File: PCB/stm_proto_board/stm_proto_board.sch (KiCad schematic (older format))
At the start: 35 parts, among them J1 Conn_01x08_Female, J2 Conn_01x04, J3 DB9_Female, J4 Conn_01x02, J5 Conn_01x04, SW1 SW_Push, SW2 SW_Push, SW3 SW_Push, SW4 SW_Push, U1 STM32F103C8T6_shield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

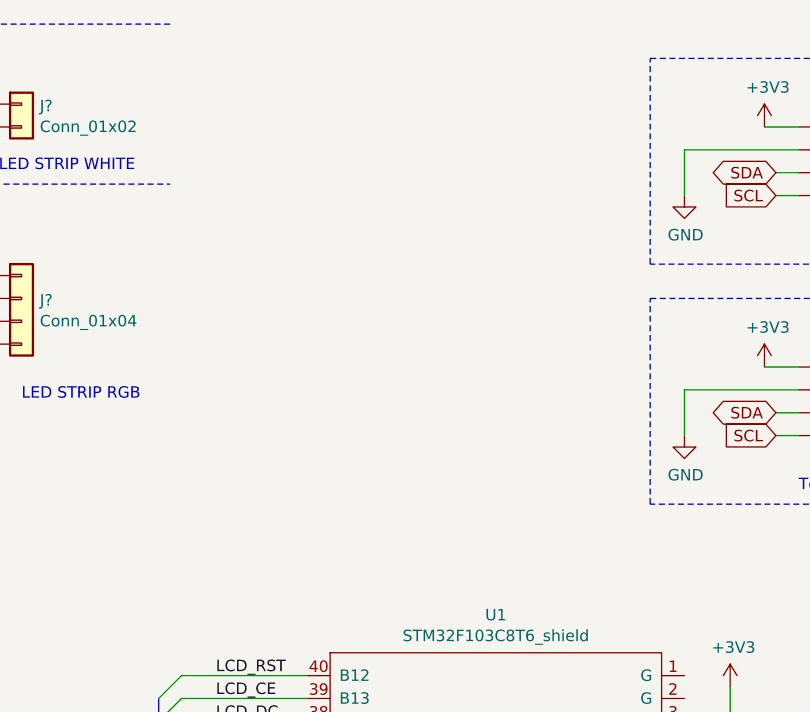
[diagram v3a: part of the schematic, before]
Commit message: Add enc28j60 on schematic + convert pinout in md format
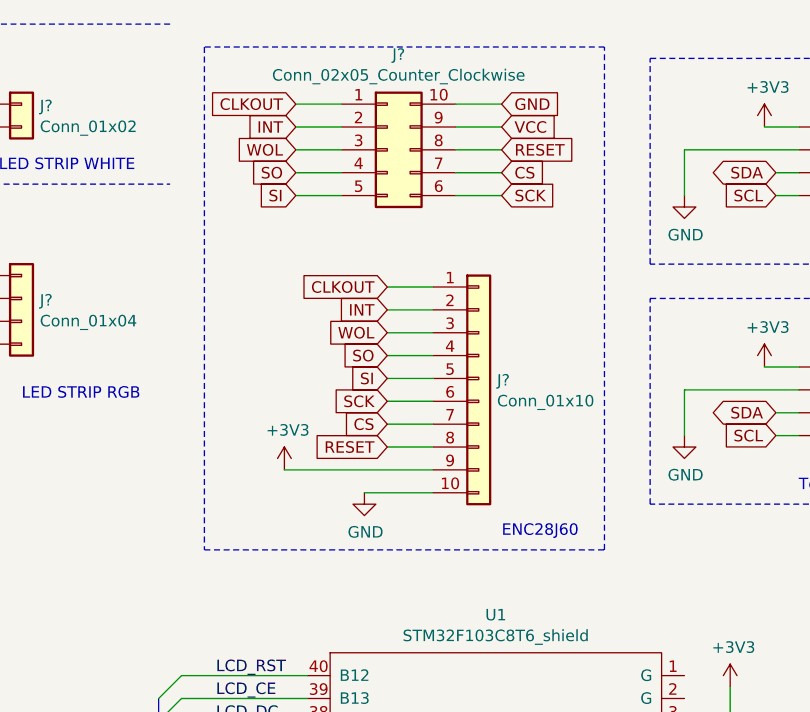
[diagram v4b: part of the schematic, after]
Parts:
- added J?: Conn_02x05_Counter_Clockwise, symbol Connector_Generic:Conn_02x05_Counter_Clockwise
- added J?: Conn_01x10, symbol Connector_Generic:Conn_01x10
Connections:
- net +3V3: now also J?.9 (Pin_9), J?.9 (Pin_9)
- net GND: now also J?.10 (Pin_10), J?.10 (Pin_10)
- new net CLKOUT: J?.1 (Pin_1), J?.1 (Pin_1)
- new net CS: J?.7 (Pin_7), J?.7 (Pin_7)
- new net INT: J?.2 (Pin_2), J?.2 (Pin_2)
- new net RESET: J?.8 (Pin_8), J?.8 (Pin_8)
- new net SCK: J?.6 (Pin_6), J?.6 (Pin_6)
- new net SI: J?.5 (Pin_5), J?.5 (Pin_5)
- new net SO: J?.4 (Pin_4), J?.4 (Pin_4)
- new net WOL: J?.3 (Pin_3), J?.3 (Pin_3)
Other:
- note added: "ENC28J60"
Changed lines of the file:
@@
 Wire Wire Line
 	1300 3050 1450 3050
-$Comp
-L power:GND #PWR0129
-U 1 1 5BB06CFC
-P 3200 2000
-F 0 "#PWR0129" H 3200 1750 50  0001 C CNN
-F 1 "GND" H 3205 1827 50  0000 C CNN
-F 2 "" H 3200 2000 50  0001 C CNN
-F 3 "" H 3200 2000 50  0001 C CNN
-	1    3200 2000
-	1    0    0    -1
-$EndComp
-Text Notes 3450 2150 0    50   ~ 0
-LED STRIP RGB
-$Comp
-L Connector_Generic:Conn_01x04 J?
-U 1 1 5BB06CEF
-P 3450 1700
-F 0 "J?" H 3530 1692 50  0000 L CNN
-F 1 "Conn_01x04" H 3530 1601 50  0000 L CNN
-F 2 "Connector_Wire:SolderWirePad_1x04_P3.81mm_Drill1mm" H 3450 1700 50  0001 C CNN
-F 3 "~" H 3450 1700 50  0001 C CNN
-	1    3450 1700
-	1    0    0    -1
-$EndComp
 Wire Wire Line
 	3250 1900 3200 1900
-Wire Wire Line
-	3200 1900 3200 2000
 Wire Wire Line
 	9650 4900 9650 4600
@@
 Text Label 2900 850  0    50   ~ 0
 OUT_W
+Text Notes 3450 2150 0    50   ~ 0
+LED STRIP RGB
+$Comp
+L Connector_Generic:Conn_02x05_Counter_Clockwise J?
+U 1 1 5E5DE981
+P 5050 1050
+F 0 "J?" H 5100 1467 50  0000 C CNN
+F 1 "Conn_02x05_Counter_Clockwise" H 5100 1376 50  0000 C CNN
+F 2 "" H 5050 1050 50  0001 C CNN
+F 3 "~" H 5050 1050 50  0001 C CNN
+	1    5050 1050
+	1    0    0    -1
+$EndComp
+Text GLabel 4650 850  0    50   Input ~ 0
+CLKOUT
+Text GLabel 4650 950  0    50   Input ~ 0
+INT
+Text GLabel 4650 1050 0    50   Input ~ 0
+WOL
+Text GLabel 4650 1150 0    50   Input ~ 0
+SO
+Text GLabel 4650 1250 0    50   Input ~ 0
+SI
+Text GLabel 5550 1250 2    50   Input ~ 0
+SCK
+Text GLabel 5550 1150 2    50   Input ~ 0
+CS
+Text GLabel 5550 1050 2    50   Input ~ 0
+RESET
+Text GLabel 5550 950  2    50   Input ~ 0
+VCC
+Text GLabel 5550 850  2    50   Input ~ 0
+GND
+$Comp
+L Connector_Generic:Conn_01x10 J?
+U 1 1 5E607F6F
+P 5450 2050
+F 0 "J?" H 5530 2042 50  0000 L CNN
+F 1 "Conn_01x10" H 5530 1951 50  0000 L CNN
+F 2 "" H 5450 2050 50  0001 C CNN
+F 3 "~" H 5450 2050 50  0001 C CNN
+	1    5450 2050
+	1    0    0    -1
+$EndComp
+Text GLabel 5050 1650 0    50   Input ~ 0
+CLKOUT
+Text GLabel 5050 1750 0    50   Input ~ 0
+INT
+Text GLabel 5050 1850 0    50   Input ~ 0
+WOL
+Text GLabel 5050 1950 0    50   Input ~ 0
+SO
+Text GLabel 5050 2050 0    50   Input ~ 0
+SI
+Text GLabel 5050 2150 0    50   Input ~ 0
+SCK
+Text GLabel 5050 2250 0    50   Input ~ 0
+CS
+Text GLabel 5050 2350 0    50   Input ~ 0
+RESET
+Wire Wire Line
+	5050 1650 5250 1650
+Wire Wire Line
+	5250 1750 5050 1750
+Wire Wire Line
+	5050 1850 5250 1850
+Wire Wire Line
+	5250 1950 5050 1950
+Wire Wire Line
+	5050 2050 5250 2050
+Wire Wire Line
+	5250 2150 5050 2150
+Wire Wire Line
+	5050 2250 5250 2250
+Wire Wire Line
+	5250 2350 5050 2350
+Wire Wire Line
+	4650 850  4850 850
+Wire Wire Line
+	4850 950  4650 950
+Wire Wire Line
+	4650 1050 4850 1050
+Wire Wire Line
+	4850 1150 4650 1150
+Wire Wire Line
+	4650 1250 4850 1250
+Wire Wire Line
+	5350 850  5550 850
+Wire Wire Line
+	5350 950  5550 950
+Wire Wire Line
+	5350 1050 5550 1050
+Wire Wire Line
+	5550 1150 5350 1150
+Wire Wire Line
+	5350 1250 5550 1250
+$Comp
+L Connector_Generic:Conn_01x04 J?
+U 1 1 5BB06CEF
+P 3450 1700
+F 0 "J?" H 3530 1692 50  0000 L CNN
+F 1 "Conn_01x04" H 3530 1601 50  0000 L CNN
+F 2 "Connector_Wire:SolderWirePad_1x04_P3.81mm_Drill1mm" H 3450 1700 50  0001 C CNN
+F 3 "~" H 3450 1700 50  0001 C CNN
+	1    3450 1700
+	1    0    0    -1
+$EndComp
+Wire Wire Line
+	3200 1900 3200 2000
+$Comp
+L power:GND #PWR0129
+U 1 1 5BB06CFC
+P 3200 2000
+F 0 "#PWR0129" H 3200 1750 50  0001 C CNN
+F 1 "GND" H 3205 1827 50  0000 C CNN
+F 2 "" H 3200 2000 50  0001 C CNN
+F 3 "" H 3200 2000 50  0001 C CNN
+	1    3200 2000
+	1    0    0    -1
+$EndComp
+$Comp
+L power:GND #PWR?
+U 1 1 5E7114CE
+P 4950 2550
+F 0 "#PWR?" H 4950 2300 50  0001 C CNN
+F 1 "GND" H 4955 2377 50  0000 C CNN
+F 2 "" H 4950 2550 50  0001 C CNN
+F 3 "" H 4950 2550 50  0001 C CNN
+	1    4950 2550
+	1    0    0    -1
+$EndComp
+$Comp
+L power:+3V3 #PWR?
+U 1 1 5E7222D3
+P 4600 2450
+F 0 "#PWR?" H 4600 2300 50  0001 C CNN
+F 1 "+3V3" H 4615 2623 50  0000 C CNN
+F 2 "" H 4600 2450 50  0001 C CNN
+F 3 "" H 4600 2450 50  0001 C CNN
+	1    4600 2450
+	1    0    0    -1
+$EndComp
+Wire Wire Line
+	4600 2450 5250 2450
+Wire Wire Line
+	4950 2550 5250 2550
+Wire Notes Line
+	4250 600  4250 2800
+Wire Notes Line
+	4250 2800 6000 2800
+Wire Notes Line
+	6000 2800 6000 600
+Wire Notes Line
+	6000 600  4250 600
+Text Notes 5550 2750 0    50   ~ 0
+ENC28J60
 Wire Bus Line
 	4050 3450 4050 5500
